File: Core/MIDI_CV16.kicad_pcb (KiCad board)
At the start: 2 copper layers, 59.5 x 99.5 mm, 167 parts, among them J1 USB_C_Receptacle_USB2.0, J2 Conn_01x06_Male, J20 Conn_02x08_Odd_Even, J3 Conn_01x10_Female, J4 Conn_01x10_Female, J5 Conn_01x04, J7 Conn_01x10_Female, J8 Conn_01x10_Female, Q1 BSS84, Q10 BSS84, Q11 2N7002, Q12 2N7002, Q13 BSS84, Q14 2N7002, Q15 BSS84, Q16 BSS84, Q17 2N7002, Q2 BSS84, Q3 2N7002, Q4 BSS84, Q5 BSS84, Q6 2N7002, Q7 BSS84, Q8 2N7002, Q9 BSS84, SW1 SW_Push_DPDT, SW2 SW_SPST, SW3 SW_SPST, U1 RP2040, U10 TL072, U11 TL072, U12 TL072, U13 MCP2517FD-xSL, U14 TLE9250V, U15 MAX5134, U16 CAT25640, U17 IS25LP032D, U2 TMUX4052, U3 MIC5504-3.3YM5, U4 TL072, U5 TL072, U6 TL072, U7 TL072, U8 TMUX4052, U9 TL072, Y1 20MHz, Y2 ECS-120-18-33-JGN-TR3

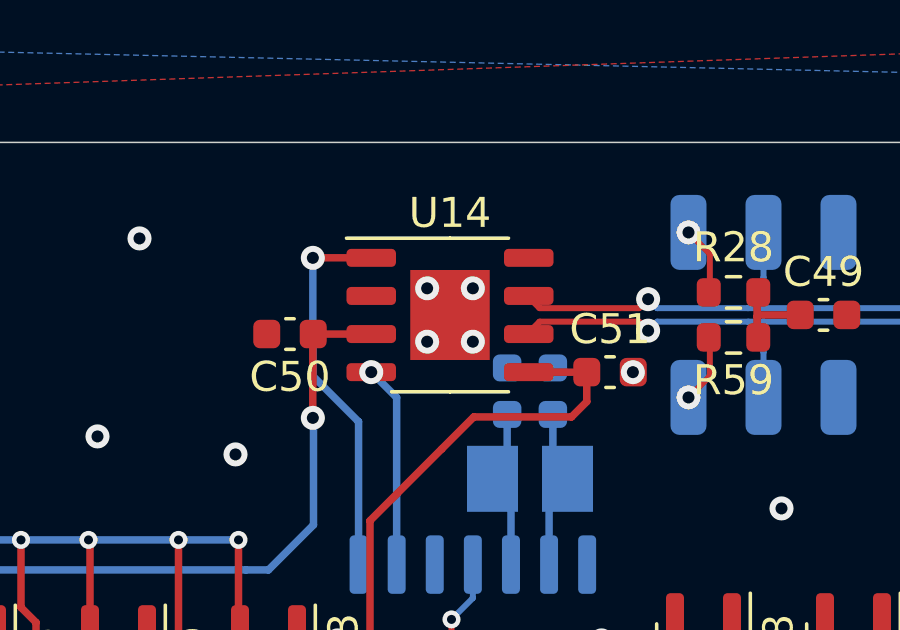
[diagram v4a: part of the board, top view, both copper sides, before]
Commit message: Change CAN tranceiver to MCP2562
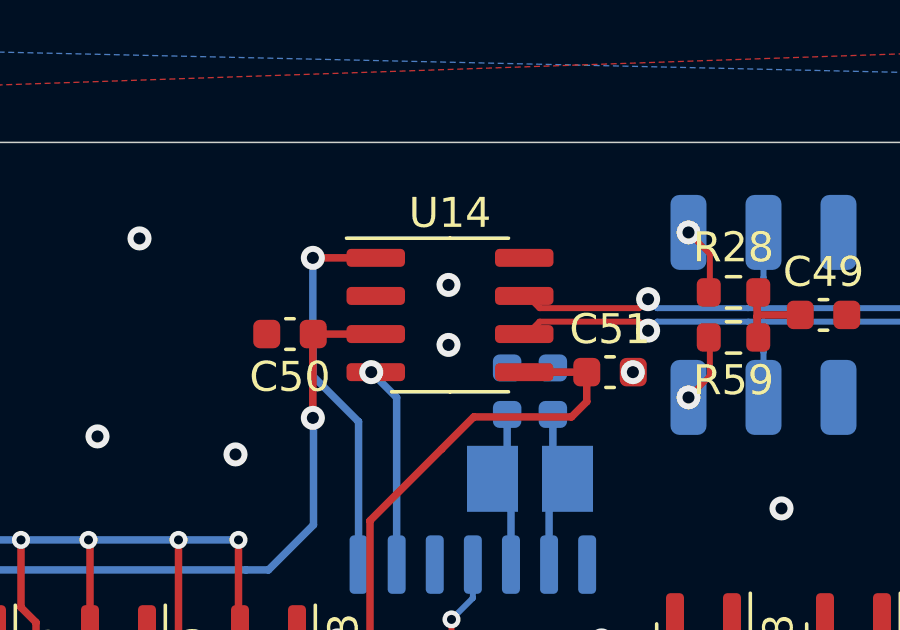
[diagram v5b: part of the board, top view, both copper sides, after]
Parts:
- Q15, Q16: value BSS84 -> ZXMP3A13FTA
- Q17: value 2N7002 -> PMV88ENER
- U14: value TLE9250V -> MCP2562FD-ESN; footprint Package_SO:Infineon_PG-DSO-8-27_3.9x4.9mm_EP2.65x3mm -> Package_SO:SOIC-8_3.9x4.9mm_P1.27mm
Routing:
- net GND: vias 137 -> 135
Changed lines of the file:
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@@
     )
   )
-  (footprint "Package_SO:Infineon_PG-DSO-8-27_3.9x4.9mm_EP2.65x3mm" (layer "F.Cu")
+  (footprint "Package_SO:SOIC-8_3.9x4.9mm_P1.27mm" (layer "F.Cu")
     (at 82.55 55.753)
-    (descr "Infineon  PG-DSO, 8 Pin (https://www.infineon.com/cms/en/product/packages/PG-DSO/PG-DSO-8-27), generated with kicad-footprint-generator ipc_gullwing_generator.py")
-    (tags "Infineon PG-DSO SO")
+    (descr "SOIC, 8 Pin (JEDEC MS-012AA, https://www.analog.com/media/en/package-pcb-resources/package/pkg_pdf/soic_narrow-r/r_8.pdf), generated with kicad-footprint-generator ipc_gullwing_generator.py")
+    (tags "SOIC SO")
     (property "Sheetfile" "MIDI_CV16.kicad_sch")
     (property "Sheetname" "")
-    (property "ki_description" "CAN FD Transceiver with Silent Mode, up to 8 Mbps, DFN-8")
-    (property "ki_keywords" "CAN FD Transceiver")
+    (property "ki_description" "High-Speed CAN Transceiver, 1Mbps, 5V supply, Vio pin, -40C to +125C, SOIC-8")
+    (property "ki_keywords" "High-Speed CAN Transceiver")
     (attr smd)
-    (fp_text reference "U14" (at 0 -3.4 180) (layer "F.SilkS")
+    (fp_text reference "U14" (at 0 -3.4) (layer "F.SilkS")
         (effects (font (size 1 1) (thickness 0.15)))
     )
-    (fp_text value "TLE9250V" (at 0 3.4 180) (layer "F.Fab")
+    (fp_text value "MCP2562FD-ESN" (at 0 3.4) (layer "F.Fab")
         (effects (font (size 1 1) (thickness 0.15)))
     )
-    (fp_text user "${REFERENCE}" (at 0 0 180) (layer "F.Fab")
+    (fp_text user "${REFERENCE}" (at 0 0) (layer "F.Fab")
         (effects (font (size 0.98 0.98) (thickness 0.15)))
     )
@@
     (fp_line (start 1.95 2.45) (end -1.95 2.45)
       (stroke (width 0.1) (type solid)) (layer "F.Fab"))
-    (pad "" smd roundrect (at -0.66 -0.75) (size 1.07 1.21) (layers "F.Paste") (roundrect_rratio 0.233645))
-    (pad "" smd roundrect (at -0.66 0.75) (size 1.07 1.21) (layers "F.Paste") (roundrect_rratio 0.233645))
-    (pad "" smd roundrect (at 0.66 -0.75) (size 1.07 1.21) (layers "F.Paste") (roundrect_rratio 0.233645))
-    (pad "" smd roundrect (at 0.66 0.75) (size 1.07 1.21) (layers "F.Paste") (roundrect_rratio 0.233645))
-    (pad "1" smd roundrect (at -2.625 -1.905) (size 1.65 0.6) (layers "F.Cu" "F.Paste" "F.Mask") (roundrect_rratio 0.25)
+    (pad "1" smd roundrect (at -2.475 -1.905) (size 1.95 0.6) (layers "F.Cu" "F.Paste" "F.Mask") (roundrect_rratio 0.25)
       (net 139 "Net-(U13-TXCAN)") (pinfunction "TXD") (pintype "input"))
-    (pad "2" smd roundrect (at -2.625 -0.635) (size 1.65 0.6) (layers "F.Cu" "F.Paste" "F.Mask") (roundrect_rratio 0.25)
+    (pad "2" smd roundrect (at -2.475 -0.635) (size 1.95 0.6) (layers "F.Cu" "F.Paste" "F.Mask") (roundrect_rratio 0.25)
       (net 1 "GND") (pinfunction "VSS") (pintype "power_in"))
-    (pad "3" smd roundrect (at -2.625 0.635) (size 1.65 0.6) (layers "F.Cu" "F.Paste" "F.Mask") (roundrect_rratio 0.25)
+    (pad "3" smd roundrect (at -2.475 0.635) (size 1.95 0.6) (layers "F.Cu" "F.Paste" "F.Mask") (roundrect_rratio 0.25)
       (net 2 "+5V") (pinfunction "VDD") (pintype "power_in"))
-    (pad "4" smd roundrect (at -2.625 1.905) (size 1.65 0.6) (layers "F.Cu" "F.Paste" "F.Mask") (roundrect_rratio 0.25)
+    (pad "4" smd roundrect (at -2.475 1.905) (size 1.95 0.6) (layers "F.Cu" "F.Paste" "F.Mask") (roundrect_rratio 0.25)
       (net 140 "Net-(U13-RXCAN)") (pinfunction "RXD") (pintype "output"))
-    (pad "5" smd roundrect (at 2.625 1.905) (size 1.65 0.6) (layers "F.Cu" "F.Paste" "F.Mask") (roundrect_rratio 0.25)
-      (net 18 "+3V3") (pinfunction "VIO") (pintype "power_in"))
-    (pad "6" smd roundrect (at 2.625 0.635) (size 1.65 0.6) (layers "F.Cu" "F.Paste" "F.Mask") (roundrect_rratio 0.25)
+    (pad "5" smd roundrect (at 2.475 1.905) (size 1.95 0.6) (layers "F.Cu" "F.Paste" "F.Mask") (roundrect_rratio 0.25)
+      (net 18 "+3V3") (pinfunction "Vio") (pintype "power_in"))
+    (pad "6" smd roundrect (at 2.475 0.635) (size 1.95 0.6) (layers "F.Cu" "F.Paste" "F.Mask") (roundrect_rratio 0.25)
       (net 68 "M2IDI-") (pinfunction "CANL") (pintype "bidirectional"))
-    (pad "7" smd roundrect (at 2.625 -0.635) (size 1.65 0.6) (layers "F.Cu" "F.Paste" "F.Mask") (roundrect_rratio 0.25)
+    (pad "7" smd roundrect (at 2.475 -0.635) (size 1.95 0.6) (layers "F.Cu" "F.Paste" "F.Mask") (roundrect_rratio 0.25)
       (net 69 "M2IDI+") (pinfunction "CANH") (pintype "bidirectional"))
-    (pad "8" smd roundrect (at 2.625 -1.905) (size 1.65 0.6) (layers "F.Cu" "F.Paste" "F.Mask") (roundrect_rratio 0.25)
-      (net 1 "GND") (pinfunction "S") (pintype "input"))
-    (pad "9" smd rect (at 0 0) (size 2.65 3) (layers "F.Cu" "F.Mask")
-      (net 1 "GND") (pinfunction "VSS") (pintype "passive"))
-    (model "${KICAD6_3DMODEL_DIR}/Package_SO.3dshapes/Infineon_PG-DSO-8-27_3.9x4.9mm_EP2.65x3mm.wrl"
+    (pad "8" smd roundrect (at 2.475 -1.905) (size 1.95 0.6) (layers "F.Cu" "F.Paste" "F.Mask") (roundrect_rratio 0.25)
+      (net 1 "GND") (pinfunction "STBY") (pintype "input"))
+    (model "${KICAD6_3DMODEL_DIR}/Package_SO.3dshapes/SOIC-8_3.9x4.9mm_P1.27mm.wrl"
       (offset (xyz 0 0 0))
       (scale (xyz 1 1 1))
@@
         (effects (font (size 1 1) (thickness 0.15)) (justify mirror))
     )
-    (fp_text value "2N7002" (at 0 -2.4) (layer "B.Fab")
+    (fp_text value "PMV88ENER" (at 0 -2.4) (layer "B.Fab")
         (effects (font (size 1 1) (thickness 0.15)) (justify mirror))
     )
@@
         (effects (font (size 1 1) (thickness 0.15)) (justify mirror))
     )
-    (fp_text value "BSS84" (at 0 -2.4) (layer "B.Fab")
+    (fp_text value "ZXMP3A13FTA" (at 0 -2.4) (layer "B.Fab")
         (effects (font (size 1 1) (thickness 0.15)) (justify mirror))
     )
@@
         (effects (font (size 1 1) (thickness 0.15)) (justify mirror))
     )
-    (fp_text value "BSS84" (at 0 -2.4 90) (layer "B.Fab")
+    (fp_text value "ZXMP3A13FTA" (at 0 -2.4 90) (layer "B.Fab")
         (effects (font (size 1 1) (thickness 0.15)) (justify mirror))
     )
@@
   (via (at 71.8 82) (size 0.8) (drill 0.4) (layers "F.Cu" "B.Cu") (free) (net 1))
   (via (at 83.4 124) (size 0.8) (drill 0.4) (layers "F.Cu" "B.Cu") (free) (net 1))
-  (via (at 81.788 54.864) (size 0.8) (drill 0.4) (layers "F.Cu" "B.Cu") (net 1))
   (via (at 105.7 110.7) (size 0.8) (drill 0.4) (layers "F.Cu" "B.Cu") (free) (net 1))
   (via (at 105.6 118.4) (size 0.8) (drill 0.4) (layers "F.Cu" "B.Cu") (free) (net 1))
@@
   (via (at 79.4 87.4) (size 0.8) (drill 0.4) (layers "F.Cu" "B.Cu") (free) (net 1))
   (via (at 84.2 137.7) (size 0.8) (drill 0.4) (layers "F.Cu" "B.Cu") (net 1))
-  (via (at 83.312 54.864) (size 0.8) (drill 0.4) (layers "F.Cu" "B.Cu") (net 1))
   (via (at 108.5 99.7) (size 0.8) (drill 0.4) (layers "F.Cu" "B.Cu") (free) (net 1))
-  (via (at 81.788 56.642) (size 0.8) (drill 0.4) (layers "F.Cu" "B.Cu") (net 1))
+  (via (at 82.5 56.75) (size 0.8) (drill 0.4) (layers "F.Cu" "B.Cu") (net 1))
   (via (at 70.8 106.5) (size 0.8) (drill 0.4) (layers "F.Cu" "B.Cu") (free) (net 1))
   (via (at 55.3 106.2) (size 0.8) (drill 0.4) (layers "F.Cu" "B.Cu") (net 1))
@@
   (via (at 67.5 147.6) (size 0.8) (drill 0.4) (layers "F.Cu" "B.Cu") (free) (net 1))
   (via (at 97.2 123.6) (size 0.8) (drill 0.4) (layers "F.Cu" "B.Cu") (free) (net 1))
-  (via (at 83.312 56.642) (size 0.8) (drill 0.4) (layers "F.Cu" "B.Cu") (net 1))
+  (via (at 82.5 54.75) (size 0.8) (drill 0.4) (layers "F.Cu" "B.Cu") (net 1))
   (via (at 62.3 106.2) (size 0.8) (drill 0.4) (layers "F.Cu" "B.Cu") (net 1))
   (via (at 71.9 100.6) (size 0.8) (drill 0.4) (layers "F.Cu" "B.Cu") (free) (net 1))
